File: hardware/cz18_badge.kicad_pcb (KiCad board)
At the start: 2 copper layers, 100 x 100 mm, 21 parts, among them J1 Dev breakout, U1 NRF24L01, U2 CHQ1838

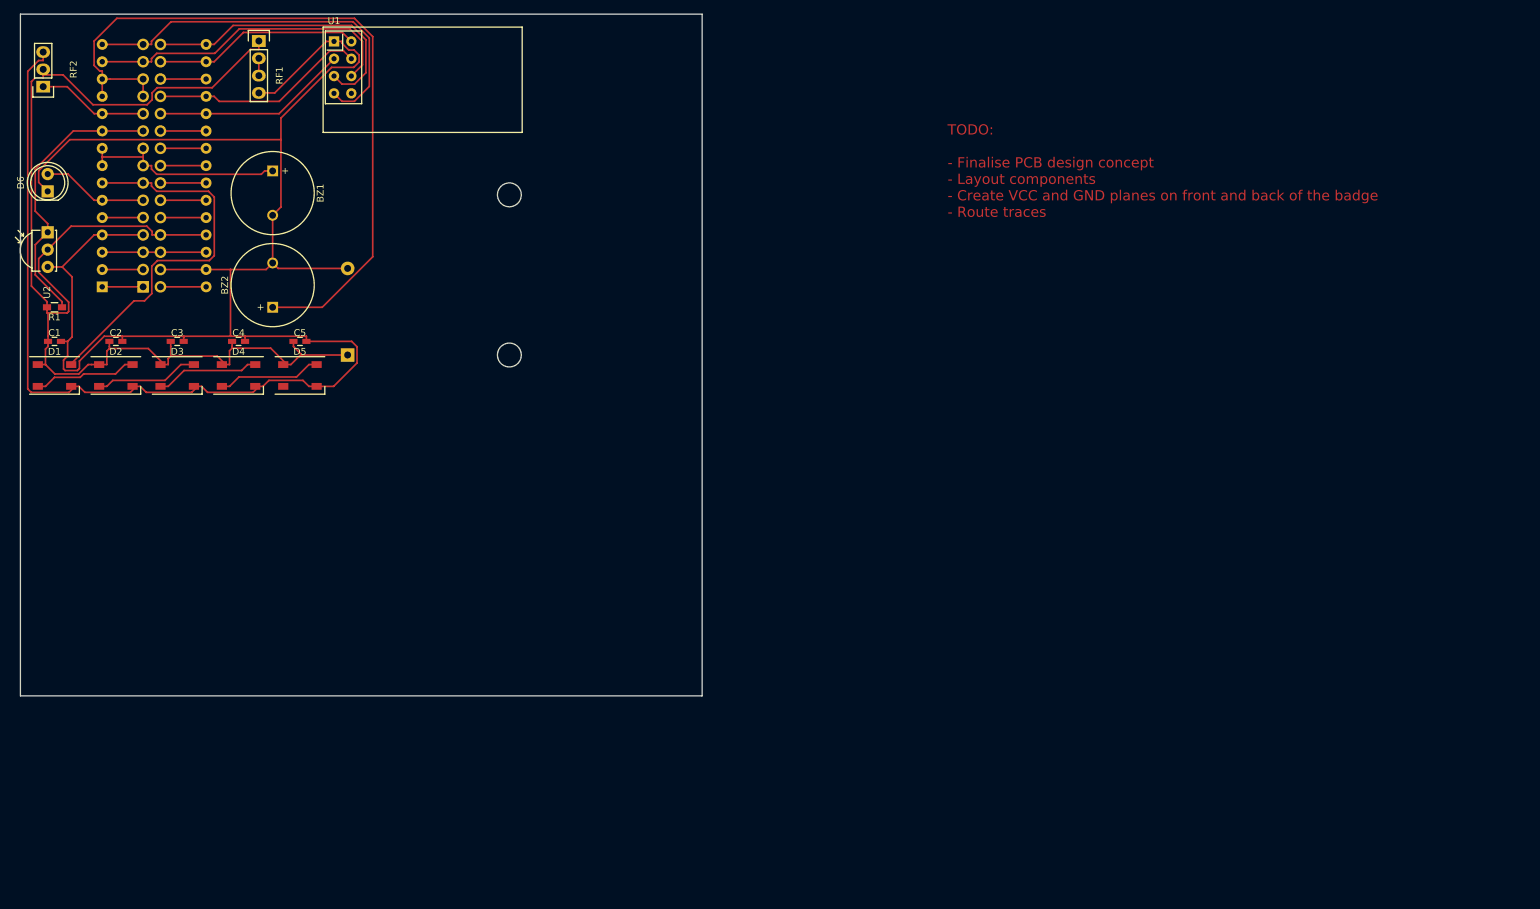
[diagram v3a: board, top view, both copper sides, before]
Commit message: Updated test PCB (single layer)
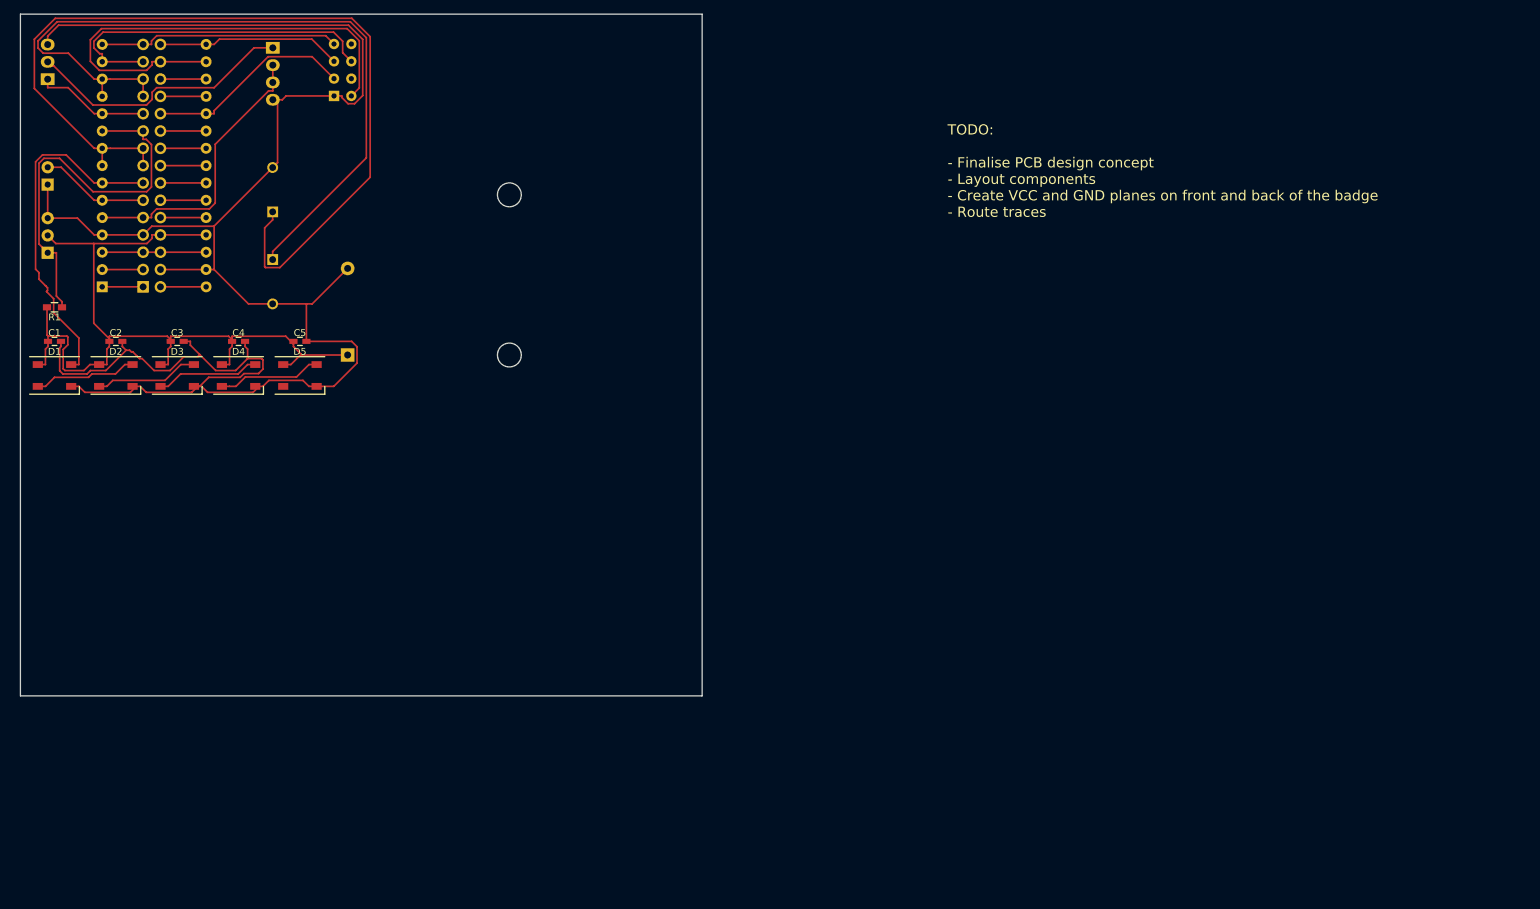
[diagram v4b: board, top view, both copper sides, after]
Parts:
- BZ1, BZ2, D6, RF1, RF2, U1, U2: moved to B.Cu
- moved U1 8.00 mm to (96.0, 42.0)
- moved BZ2 7.00 mm to (87.0, 66.0), turned to 270 degrees
- moved BZ1 6.00 mm to (87.0, 59.0), turned to 90 degrees
- moved U2 3.00 mm to (54.0, 65.0), turned to 90 degrees
- moved RF1 2.24 mm to (87.0, 40.0)
- moved RF2 1.28 mm to (54.0, 37.0)
- moved D6 1.00 mm to (54.0, 55.0)
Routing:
- net BUZZ1: track 31.1 -> 134.0 mm
- net 3V3: track 30.3 -> 70.9 mm
- net GND: track 326.2 -> 285.8 mm
- net D2: track 8.54 -> 41.9 mm
- net VCC: track 188.0 -> 159.6 mm
- net A0: track 31.8 -> 6.70 mm
- net D12: track 55.5 -> 35.3 mm
- net D7: track 41.5 -> 57.4 mm
- net D13: track 42.8 -> 27.1 mm
- net D4: track 56.2 -> 51.5 mm
- net D11: track 46.9 -> 50.8 mm
- net A1: track 28.8 -> 30.5 mm
- net BUZZ2: track 111.0 -> 112.2 mm
- net D8: track 16.3 -> 16.8 mm

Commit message: Implemented vectorised kong. All works, but no clearance between traces and areas. Will add manual fill zones.
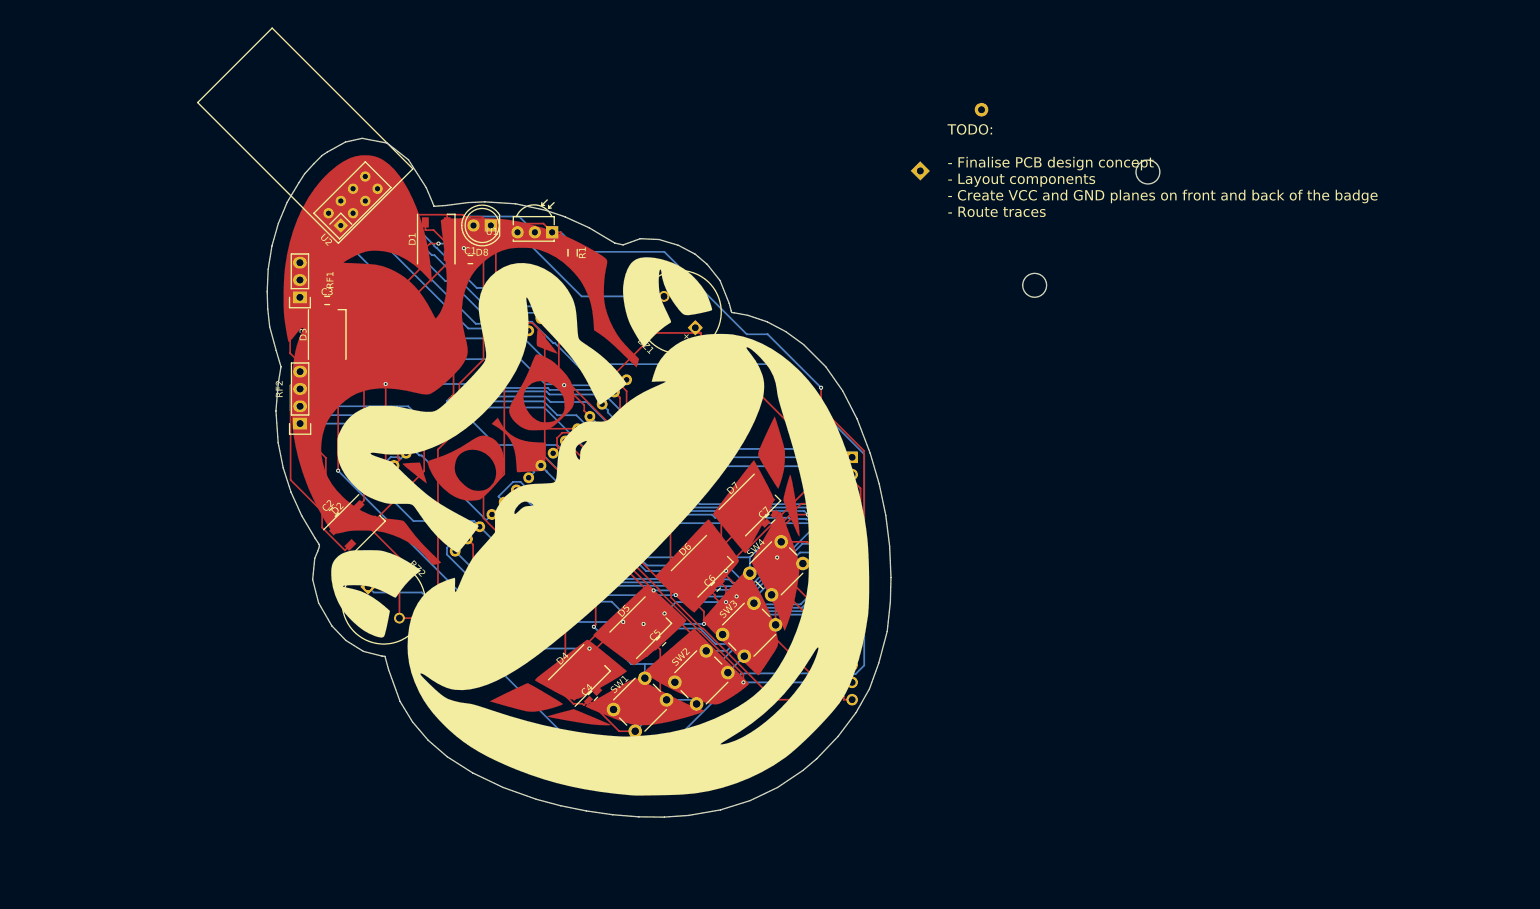
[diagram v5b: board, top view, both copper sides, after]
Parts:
- added C6: 104, Capacitors_SMD:C_0603_HandSoldering, F.Cu at (152.0, 114.0)
- added C7: 104, Capacitors_SMD:C_0603_HandSoldering, F.Cu at (160.0, 104.0)
- added COPPER: LOGO, vector-kong:Copper, F.Cu at (136.0, 98.0)
- added D7: SK6812, LED_SMD:LED_SK6812_PLCC4_5.0x5.0mm_P3.2mm, F.Cu at (157.0, 102.0)
- added D8: 940nm, LEDs:LED_D5.0mm, F.Cu at (119.0, 61.0)
- added SILK: LOGO, vector-kong:Silkscreen, F.Cu at (136.0, 98.0)
- added SW1: SW_Push, Buttons_Switches_THT:SW_PUSH_6mm_h4.3mm, F.Cu at (137.0, 132.0)
- added SW2: SW_Push, Buttons_Switches_THT:SW_PUSH_6mm_h4.3mm, F.Cu at (146.0, 128.0)
- added SW3: SW_Push, Buttons_Switches_THT:SW_PUSH_6mm_h4.3mm, F.Cu at (153.0, 121.0)
- added SW4: SW_Push, Buttons_Switches_THT:SW_PUSH_6mm_h4.3mm, F.Cu at (157.0, 112.0)
- added TIN: LOGO, vector-kong:Tin, F.Cu at (136.0, 98.0)
- BZ1, BZ2: moved to F.Cu
- D6: value 940nm -> SK6812; footprint LEDs:LED_D5.0mm -> LED_SMD:LED_SK6812_PLCC4_5.0x5.0mm_P3.2mm; moved to F.Cu
- RF1: value 433MHz Receiver -> 433MHz Transmitter; footprint Sensors:RF_Receiver_433_MHz -> Sensors:RF_Transmitter_433_MHz; moved to F.Cu
- RF2: value 433MHz Transmitter -> 433MHz Receiver; footprint Sensors:RF_Transmitter_433_MHz -> Sensors:RF_Receiver_433_MHz; moved to F.Cu
- U1: value NRF24L01 -> CHQ1838; footprint RF_Modules:nRF24L01_Breakout -> Opto-Devices:IRReceiver_Vishay_MOLD-3pin; moved to F.Cu
- U2: value CHQ1838 -> NRF24L01; footprint Opto-Devices:IRReceiver_Vishay_MOLD-3pin -> RF_Modules:nRF24L01_Breakout; moved to F.Cu
- moved D6 111.1 mm to (150.0, 111.0), turned to 45 degrees
- moved J1 107.0 mm to (172.0, 95.0), turned to 180 degrees
- moved BT1 88.2 mm to (182.0, 53.0), turned to 315 degrees
- moved R1 76.4 mm to (131.0, 65.0), turned to 270 degrees
- moved C4 73.5 mm to (134.0, 130.0), turned to 45 degrees
- moved C5 68.9 mm to (144.0, 122.0), turned to 45 degrees
- moved D4 66.6 mm to (132.0, 127.0), turned to 45 degrees
- moved BZ1 64.3 mm to (149.0, 76.0), turned to 135 degrees
- moved D5 62.2 mm to (141.0, 120.0), turned to 45 degrees
- moved C1 62.2 mm to (116.0, 66.0)
- moved RF2 60.6 mm to (91.0, 85.0)
- moved D1 59.5 mm to (111.0, 63.0), turned to 90 degrees
- moved BZ2 50.0 mm to (101.0, 114.0), turned to 315 degrees
- moved A1 49.6 mm to (103.0, 98.0), turned to 315 degrees
- moved U2 43.2 mm to (97.0, 61.0), turned to 135 degrees
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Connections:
- D5 pad 4: (no net) -> Net-(D5-Pad4)
- D6 pad 2: D3 -> Net-(D5-Pad4)
- RF1 pad 1: VCC -> D8
- RF1 pad 2: D2 -> VCC
- RF1 pad 3: D2 -> GND
- RF2 pad 1: D8 -> VCC
- RF2 pad 2: VCC -> D2
- RF2 pad 3: GND -> D2
- U1 pad 1: GND -> D7
- U1 pad 2: 3V3 -> VCC
- U1 pad 3: A1 -> GND
- U2 pad 1: D7 -> GND
- U2 pad 2: VCC -> 3V3
- U2 pad 3: GND -> A1
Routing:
- net VCC: track 159.6 -> 292.0 mm, vias 0 -> 2
- net D8: track 16.8 -> 134.3 mm, vias 0 -> 2
- net A0: track 6.70 -> 121.5 mm, vias 0 -> 2
- net D3: track 16.0 -> 105.7 mm
- net D13: track 27.1 -> 115.4 mm
- net A1: track 30.5 -> 117.4 mm, vias 0 -> 3
- net RESET: track 15.2 -> 100.0 mm
- net D12: track 35.3 -> 117.7 mm, vias 0 -> 2
- net TX: track 6.00 -> 87.3 mm, vias 0 -> 1
- net D11: track 50.8 -> 125.6 mm
- net VIN: track 6.70 -> 79.7 mm, vias 0 -> 2
- net RX: track 6.00 -> 78.2 mm, vias 0 -> 3
- net A2: track 6.70 -> 78.5 mm, vias 0 -> 1
- net A3: track 6.70 -> 73.8 mm
- net D7: track 57.4 -> 118.7 mm, vias 0 -> 1
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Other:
- board size 100 x 100 mm -> 91.5 x 99.6 mm

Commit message: Improved PCB annotation, working on manual fill zone colouring
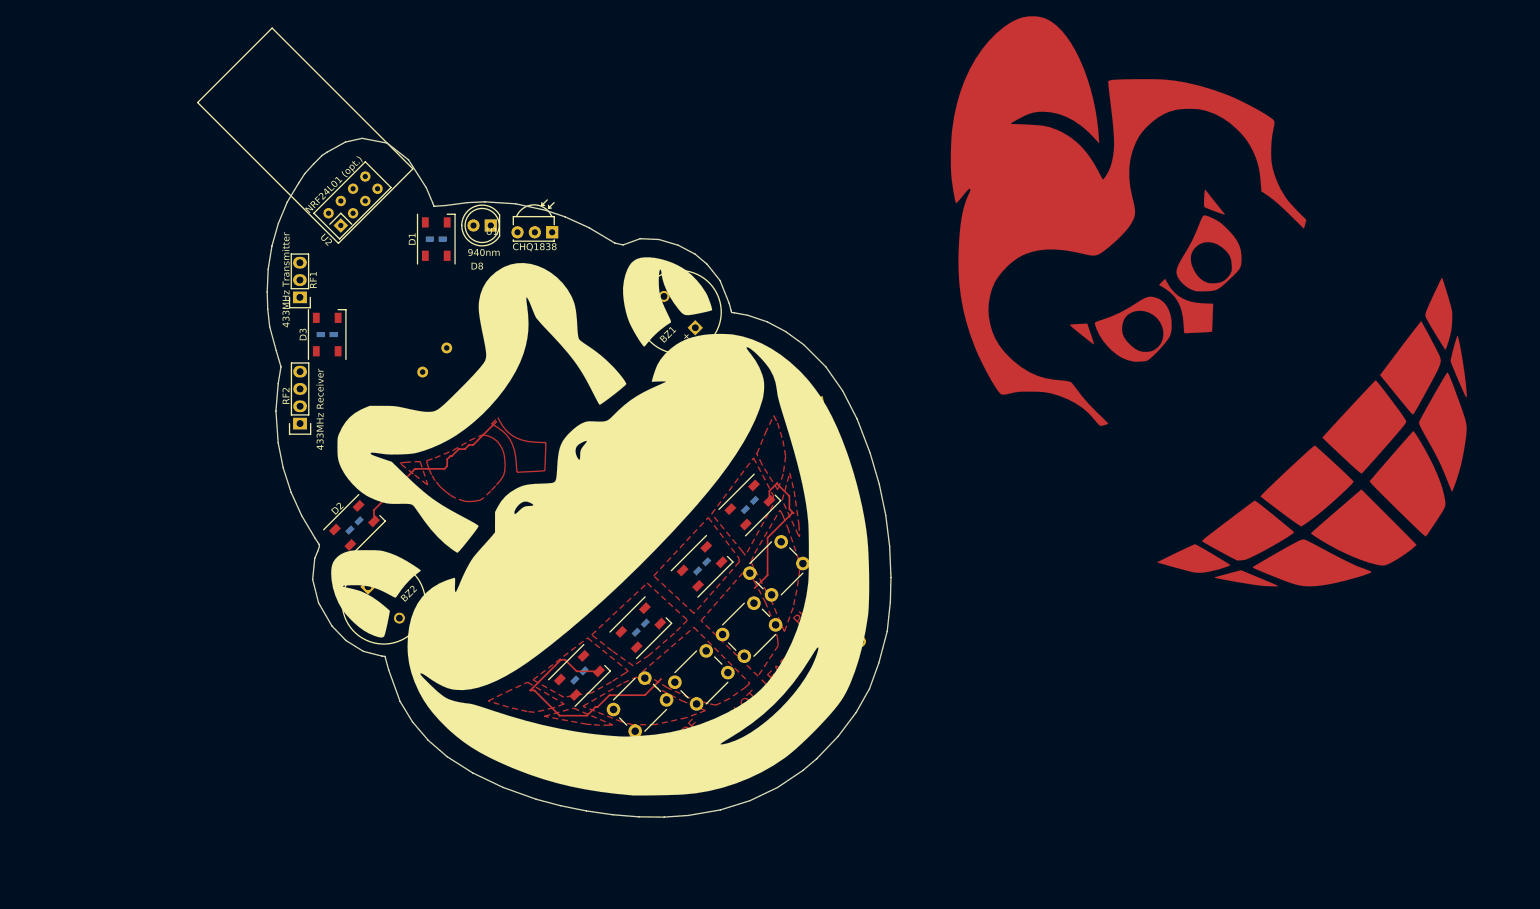
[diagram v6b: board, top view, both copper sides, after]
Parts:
- removed A1: Arduino_Nano_v3.x, Modules:Arduino_Nano
- removed BT1: Battery, Battery_Holders:Keystone_2479_3xAAA
- added C8: 100uf (opt.), Capacitors_THT:C_Disc_D5.0mm_W2.5mm_P5.00mm, B.Cu at (109.0, 82.5)
- added J2: VCC (max 5V), Pin_Headers:Pin_Header_Straight_1x01_Pitch2.54mm, B.Cu at (124.0, 104.0)
- added J3: GND, Pin_Headers:Pin_Header_Straight_1x01_Pitch2.54mm, B.Cu at (134.0, 94.0)
- added X1: #Badgelife Shitty AddOn (opt.), ShittyAddOn:Badgelife-Shitty-2x2, F.Cu at (115.0, 122.0)
- BZ1, BZ2: value Buzzer -> (none)
- C1, C2, C3, C4, C5, C6, C7: value 104 -> 0.1uf (opt.); moved to B.Cu
- J1: value Dev breakout -> Dev breakout (opt.)
- R1: moved to B.Cu
- SW1: value SW_Push -> MODE
- SW2: value SW_Push -> SLOT
- SW3: value SW_Push -> LEARN
- SW4: value SW_Push -> PLAY
- U2: value NRF24L01 -> NRF24L01 (opt.)
- moved COPPER 100.0 mm to (233.9, 77.6)
- moved J1 9.43 mm to (167.0, 87.0), turned to 190 degrees
- moved R1 6.71 mm to (125.0, 68.0), turned to 0 degrees
- moved C1 5.83 mm to (111.0, 63.0)
- moved C3 5.00 mm to (95.0, 77.0)
- moved C2 3.61 mm to (99.0, 105.0)
- moved C4 3.61 mm to (132.0, 127.0)
- moved C5 3.61 mm to (141.0, 120.0)
- moved C6 3.61 mm to (150.0, 111.0)
- moved C7 3.61 mm to (157.0, 102.0)
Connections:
- D7 pad 4: (no net) -> Net-(D7-Pad4)
- SW3 pad 1: A4 -> A6
- SW4 pad 1: A5 -> A7
- U2 pad 8: (no net) -> Net-(U2-Pad8)
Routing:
- net VCC: track 292.0 -> 0.00 mm, vias 2 -> 0
- net GND: track 294.3 -> 83.3 mm, vias 3 -> 0
- net BUZZ2: track 135.4 -> 0.00 mm, vias 1 -> 0
- net D8: track 134.3 -> 0.00 mm, vias 2 -> 0
- net D11: track 125.6 -> 0.00 mm
- net A0: track 121.5 -> 0.00 mm, vias 2 -> 0
- net D7: track 118.7 -> 0.00 mm, vias 1 -> 0
- net D12: track 117.7 -> 0.00 mm, vias 2 -> 0
- net 3V3: track 117.6 -> 0.00 mm, vias 1 -> 0
- net A1: track 117.4 -> 0.00 mm, vias 3 -> 0
- net D13: track 115.4 -> 0.00 mm
- net D3: track 105.7 -> 0.00 mm
- net RESET: track 100.0 -> 0.00 mm
- net D4: track 99.2 -> 0.00 mm, vias 1 -> 0
- net D2: track 98.0 -> 0.00 mm, vias 1 -> 0
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- added copper zone on F.Cu, net GND
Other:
- board text added: "LEARN"
- board text added: "MODE"
- board text added: "PLAY"
- board text added: "SLOT"
- board text removed: "TODO: - Finalise PCB design concept - Layout components - Create VCC and GND planes on front and back of the badge - Route traces"

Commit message: Minor fixes
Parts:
- added A1: Arduino Nano v3.x, ArduinoNanoCustom:Arduino_Nano, B.Cu at (101.9, 98.1)
- added J4: LEDS OUT, Pin_Headers:Pin_Header_Straight_1x01_Pitch2.54mm, F.Cu at (131.9, 157.8)
- added REF**: AA Battery holder silkscreen, BatteryHolder:AA_Battery_holder_silkscreen, F.Cu at (135.5, 146.5)
- BZ1, BZ2: value (none) -> Buzzer

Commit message: Added lanyard hole, annotated dev headers, moved components
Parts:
- removed COPPER: LOGO, vector-kong:Copper
- added REF**: MountingHole_4.3mm_M4_Pad_Via, Mounting_Holes:MountingHole_4.3mm_M4_Pad_Via, F.Cu at (92.7, 62.2)
- D1: value SK6812 -> Infrared
- D3: value SK6812 -> 433MHz RF
- J4: moved to B.Cu
- moved J4 80.5 mm to (163.8, 84.0), turned to 190 degrees
- moved BATT 74.2 mm to (143.8, 72.8), turned to 225 degrees
- moved C2 61.8 mm to (155.5, 80.0), turned to 315 degrees
- moved D2 58.0 mm to (152.5, 82.5)
- moved RF1 9.55 mm to (92.0, 78.5)
- moved RF2 8.63 mm to (92.5, 93.5)
- moved C3 8.54 mm to (98.0, 85.0)
- moved D3 8.54 mm to (98.0, 85.0)
- moved U2 6.95 mm to (97.2, 54.0), turned to 45 degrees
- renumbered REF** to BATT
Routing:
- net GND: track 83.3 -> 0.00 mm
- added copper zone on B.Cu, net GND
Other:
- board text added: "3V3"
- board text added: "A0"
- board text added: "A1"
- board text added: "A2"
- board text added: "A3"
- board text added: "A4"
- board text added: "A5"
- board text added: "A6"
- board text added: "A7"
- board text added: "AREF"
- board text added: "Buzzers"
- board text added: "D10"
- board text added: "D11"
- board text added: "D12"
- board text added: "D13"
- board text added: "D7"
- board text added: "D8"
- board text added: "D9"
- board text added: "GND"
- board text added: "RST"
- board text added: "VCC"
- board text added: "VIN"
